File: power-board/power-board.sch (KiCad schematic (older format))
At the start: 36 parts, among them J1 ECS00066, J11 ECS00059, J8 ECS00059, J9 ECS00059, P1 ECS00067, P12 ECS00068, P13 ECS00068, P2 ECS00007, P3 ECS00013, P4 ECS00004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

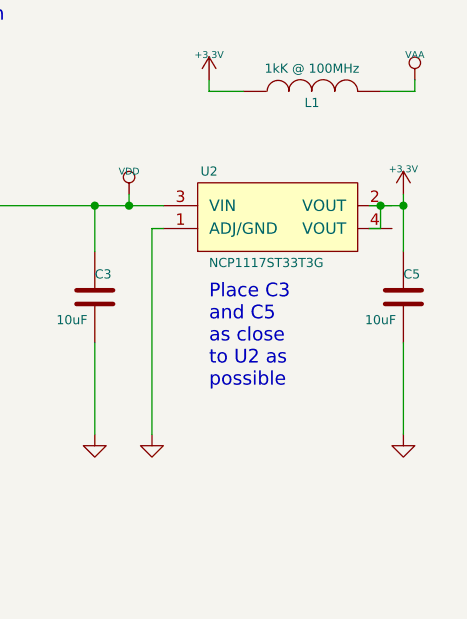
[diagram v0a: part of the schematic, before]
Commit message: Commiting power board output files.
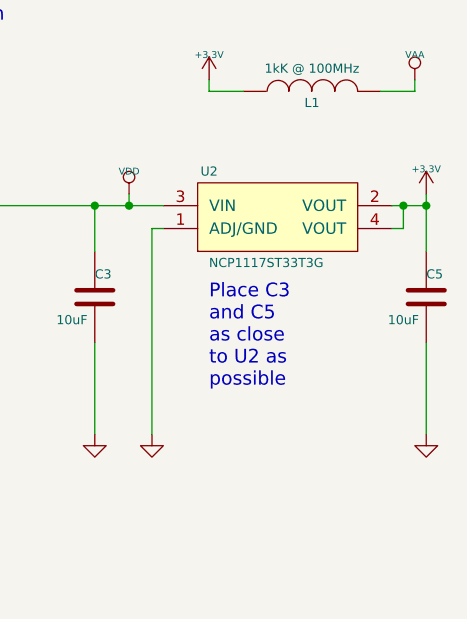
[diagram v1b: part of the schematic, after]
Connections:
- net +3V3: now also U2.2 (VOUT), U2.4 (VOUT)
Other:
- moved on the sheet: C5
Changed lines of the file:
@@
 Date "2020-04-25"
 Rev "C"
-Comp "Project: Buoy Instrumentation"
+Comp "Project: Instrumentation Buoy"
 Comment1 "Drawn by: Andrew Li"
 Comment2 ""
@@
 	9550 5150 9600 5150
 Wire Wire Line
-	10500 5050 10550 5050
-Wire Wire Line
-	10550 5050 10650 5050
-Wire Wire Line
-	10500 5150 10550 5150
-Wire Wire Line
-	10550 5150 10550 5050
-Connection ~ 10550 5050
-Wire Wire Line
-	10650 5000 10650 5050
-Wire Wire Line
-	10650 5050 10650 5250
+	10750 5000 10750 5050
+Wire Wire Line
+	10750 5050 10750 5250
 $Comp
 L power:+3.3V #PWR012
 U 1 1 53B80115
-P 10650 5000
-F 0 "#PWR012" H 10650 4960 30  0001 C CNN
-F 1 "+3.3V" H 10650 5110 30  0000 C CNN
-F 2 "~" H 10650 5000 60  0000 C CNN
-F 3 "~" H 10650 5000 60  0000 C CNN
-	1    10650 5000
-	1    0    0    -1
-$EndComp
-Connection ~ 10650 5050
+P 10750 5000
+F 0 "#PWR012" H 10750 4960 30  0001 C CNN
+F 1 "+3.3V" H 10750 5110 30  0000 C CNN
+F 2 "~" H 10750 5000 60  0000 C CNN
+F 3 "~" H 10750 5000 60  0000 C CNN
+	1    10750 5000
+	1    0    0    -1
+$EndComp
+Connection ~ 10750 5050
 Text Label 3500 5050 0    60   ~ 0
 ~CHARGE
@@
 L Capacitors:ECS00050 C5
 U 1 1 53B8C2F4
-P 10650 5450
-F 0 "C5" H 10650 5550 40  0000 L CNN
-F 1 "ECS00050" V 10400 5300 40  0001 L CNN
-F 2 "ECFootprints:EC0805" H 10688 5300 30  0001 C CNN
-F 3 "~" H 10650 5450 60  0001 C CNN
-F 4 "10uF" H 10550 5350 40  0000 C CNN "Component Value"
-F 5 "GRM21BR61A106KE19L" V 10800 5450 40  0001 C CNN "Manfacturer Part Number"
-F 6 "Murata" V 10500 5450 40  0001 C CNN "Manufacturer"
-F 7 "GRM Series" V 10900 5450 40  0001 C CNN "Series"
-F 8 "10uF, 0805, 10%, 10V, X5R, Ceramic" V 11000 5350 40  0001 C CNN "Part Description"
-	1    10650 5450
+P 10750 5450
+F 0 "C5" H 10750 5550 40  0000 L CNN
+F 1 "ECS00050" V 10500 5300 40  0001 L CNN
+F 2 "ECFootprints:EC0805" H 10788 5300 30  0001 C CNN
+F 3 "~" H 10750 5450 60  0001 C CNN
+F 4 "10uF" H 10650 5350 40  0000 C CNN "Component Value"
+F 5 "GRM21BR61A106KE19L" V 10900 5450 40  0001 C CNN "Manfacturer Part Number"
+F 6 "Murata" V 10600 5450 40  0001 C CNN "Manufacturer"
+F 7 "GRM Series" V 11000 5450 40  0001 C CNN "Series"
+F 8 "10uF, 0805, 10%, 10V, X5R, Ceramic" V 11100 5350 40  0001 C CNN "Part Description"
+	1    10750 5450
 	1    0    0    -1
 $EndComp
@@
 L power:GND #PWR011
 U 1 1 53B80095
-P 10650 6050
-F 0 "#PWR011" H 10650 6050 30  0001 C CNN
-F 1 "GND" H 10650 5980 30  0001 C CNN
-F 2 "~" H 10650 6050 60  0000 C CNN
-F 3 "~" H 10650 6050 60  0000 C CNN
-	1    10650 6050
+P 10750 6050
+F 0 "#PWR011" H 10750 6050 30  0001 C CNN
+F 1 "GND" H 10750 5980 30  0001 C CNN
+F 2 "~" H 10750 6050 60  0000 C CNN
+F 3 "~" H 10750 6050 60  0000 C CNN
+	1    10750 6050
 	1    0    0    -1
 $EndComp
@@
 	9550 5150 9550 6050
 Wire Wire Line
-	10650 6050 10650 5650
+	10750 6050 10750 5650
 $Comp
 L power:GND #PWR0101
@@
 Text Notes 8050 4350 0    60   ~ 0
 Short P4 to connect\nCharging circuit with\nbattery
+Wire Wire Line
+	10600 5050 10650 5050
+Wire Wire Line
+	10600 5150 10650 5150
+Wire Wire Line
+	10650 5150 10650 5050
+Connection ~ 10650 5050
+Wire Wire Line
+	10650 5050 10750 5050
 $EndSCHEMATC
